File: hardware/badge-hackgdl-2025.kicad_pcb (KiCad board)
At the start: 11 copper layers, 73.4 x 79.5 mm, 61 parts, among them J1 ADDON, J2 Battery, P1 USB_C_Plug_USB2.0, Q1 DMG3415U-7, Q2 MMBT2222A, SW1 ON, SW2 RESET, SW3 BOOT, SW4 RIGHT, SW5 BACK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

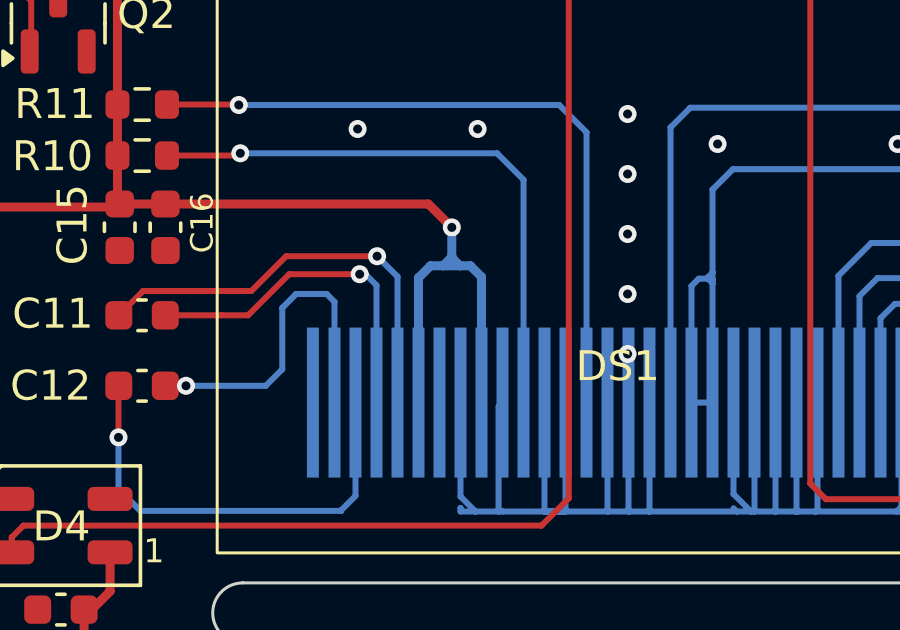
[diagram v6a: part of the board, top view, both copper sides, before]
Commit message: feat(hw): change routes in oled
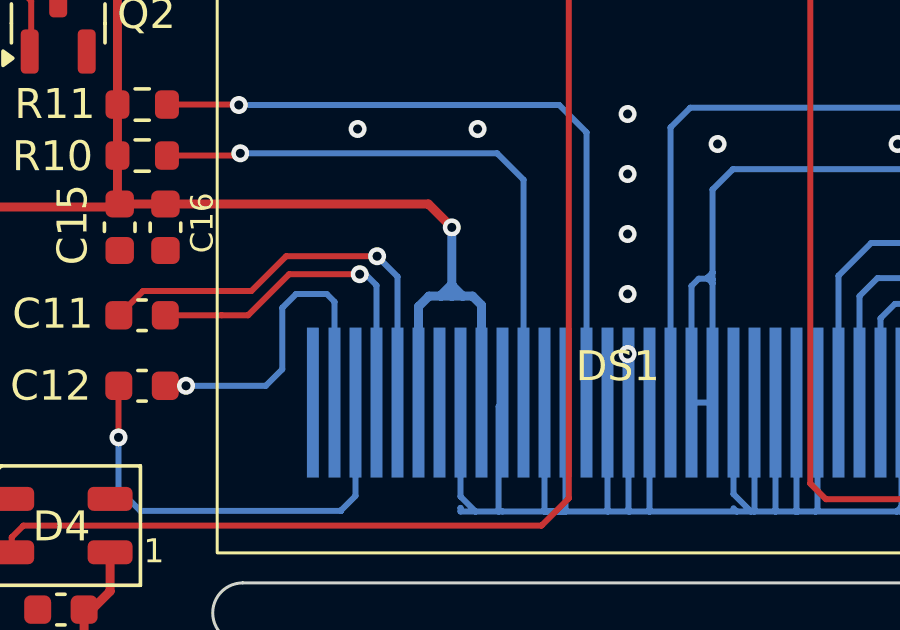
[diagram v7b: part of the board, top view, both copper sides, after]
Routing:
- net +3V3: track 251.2 -> 250.7 mm
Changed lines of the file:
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@@
 		)
 		(embedded_fonts no)
+		(model "${KIPRJMOD}/3dmodels/0.96 OLED - Flat Reverse.stp"
+			(hide yes)
+			(offset
+				(xyz 0 5.5 0)
+			)
+			(scale
+				(xyz 1 1 1)
+			)
+			(rotate
+				(xyz -0 -0 -0)
+			)
+		)
+		(model "${KIPRJMOD}/3dmodels/OLED  0.96 inch 64x128.STEP"
+			(offset
+				(xyz 2 18 -3)
+			)
+			(scale
+				(xyz 1 1 1)
+			)
+			(rotate
+				(xyz -90 -0 -0)
+			)
+		)
 	)
 	(footprint "Capacitor_SMD:C_0603_1608Metric"
@@
 	)
 	(segment
-		(start 128.14 52.74)
-		(end 128.14 52.79)
+		(start 127.78 54.07)
+		(end 127.38 54.07)
 		(width 0.3)
 		(layer "B.Cu")
@@
 	)
 	(segment
-		(start 128.14 51.78)
-		(end 128.14 52.74)
+		(start 128.14 53.68)
+		(end 128.14 54.07)
 		(width 0.3)
 		(layer "B.Cu")
@@
 	)
 	(segment
-		(start 127.85 53.06)
-		(end 127.43 53.06)
+		(start 118.42 88.57)
+		(end 119.54 88.57)
 		(width 0.3)
 		(layer "B.Cu")
@@
 	)
 	(segment
-		(start 127.43 53.06)
-		(end 127.03 53.46)
+		(start 122.945 89.89)
+		(end 122.77 89.715)
 		(width 0.3)
 		(layer "B.Cu")
@@
 	)
 	(segment
-		(start 118.42 88.57)
-		(end 119.54 88.57)
+		(start 128.14 53.71)
+		(end 128.5 54.07)
 		(width 0.3)
 		(layer "B.Cu")
@@
 	)
 	(segment
-		(start 128.14 52.79)
-		(end 128.41 53.06)
+		(start 121.16 89.205)
+		(end 120.175 89.205)
 		(width 0.3)
 		(layer "B.Cu")
@@
 	)
 	(segment
-		(start 128.12 52.79)
-		(end 127.85 53.06)
+		(start 120.175 89.205)
+		(end 119.54 88.57)
 		(width 0.3)
 		(layer "B.Cu")
@@
 	)
 	(segment
-		(start 122.945 89.89)
-		(end 122.77 89.715)
+		(start 124.921189 89.89)
+		(end 122.945 89.89)
 		(width 0.3)
 		(layer "B.Cu")
@@
 	)
 	(segment
-		(start 121.16 89.205)
-		(end 120.175 89.205)
+		(start 128.14 53.68)
+		(end 128.14 53.71)
 		(width 0.3)
 		(layer "B.Cu")
@@
 	)
 	(segment
-		(start 129.13 57.62)
-		(end 129.13 53.43)
+		(start 128.14 51.78)
+		(end 128.14 53.68)
 		(width 0.3)
 		(layer "B.Cu")
@@
 	)
 	(segment
-		(start 120.175 89.205)
-		(end 119.54 88.57)
+		(start 103.419178 53.831476)
+		(end 103.146678 53.558976)
 		(width 0.3)
 		(layer "B.Cu")
@@
 	)
 	(segment
-		(start 127.03 53.46)
-		(end 127.03 57.62)
+		(start 127.78 54.04)
+		(end 127.78 54.07)
 		(width 0.3)
 		(layer "B.Cu")
@@
 	)
 	(segment
-		(start 124.921189 89.89)
-		(end 122.945 89.89)
+		(start 127.03 54.42)
+		(end 127.03 57.62)
 		(width 0.3)
 		(layer "B.Cu")
@@
 	)
 	(segment
-		(start 128.14 52.79)
-		(end 128.12 52.79)
+		(start 128.14 54.07)
+		(end 127.78 54.07)
 		(width 0.3)
 		(layer "B.Cu")
@@
 	)
 	(segment
-		(start 103.419178 53.831476)
-		(end 103.146678 53.558976)
+		(start 122.77 89.715)
+		(end 121.67 89.715)
 		(width 0.3)
 		(layer "B.Cu")
@@
 	)
 	(segment
-		(start 128.76 53.06)
-		(end 128.41 53.06)
+		(start 129.13 54.37)
+		(end 128.83 54.07)
 		(width 0.3)
 		(layer "B.Cu")
@@
 	)
 	(segment
-		(start 122.77 89.715)
-		(end 121.67 89.715)
+		(start 151.2 85.68)
+		(end 149.135 85.68)
 		(width 0.3)
 		(layer "B.Cu")
@@
 	)
 	(segment
-		(start 128.01 53.06)
-		(end 127.85 53.06)
+		(start 129.13 57.62)
+		(end 129.13 54.37)
 		(width 0.3)
 		(layer "B.Cu")
@@
 	)
 	(segment
-		(start 151.2 85.68)
-		(end 149.135 85.68)
+		(start 128.83 54.07)
+		(end 128.5 54.07)
 		(width 0.3)
 		(layer "B.Cu")
@@
 	)
 	(segment
-		(start 117.85 88)
-		(end 118.42 88.57)
+		(start 127.38 54.07)
+		(end 127.03 54.42)
 		(width 0.3)
 		(layer "B.Cu")
@@
 	)
 	(segment
-		(start 128.14 52.74)
-		(end 128.14 52.93)
+		(start 117.85 88)
+		(end 118.42 88.57)
 		(width 0.3)
 		(layer "B.Cu")
@@
 	)
 	(segment
-		(start 128.41 53.06)
-		(end 128.01 53.06)
+		(start 128.14 53.68)
+		(end 127.78 54.04)
 		(width 0.3)
 		(layer "B.Cu")
@@
 	)
 	(segment
-		(start 129.13 53.43)
-		(end 128.76 53.06)
+		(start 128.5 54.07)
+		(end 128.14 54.07)
 		(width 0.3)
 		(layer "B.Cu")

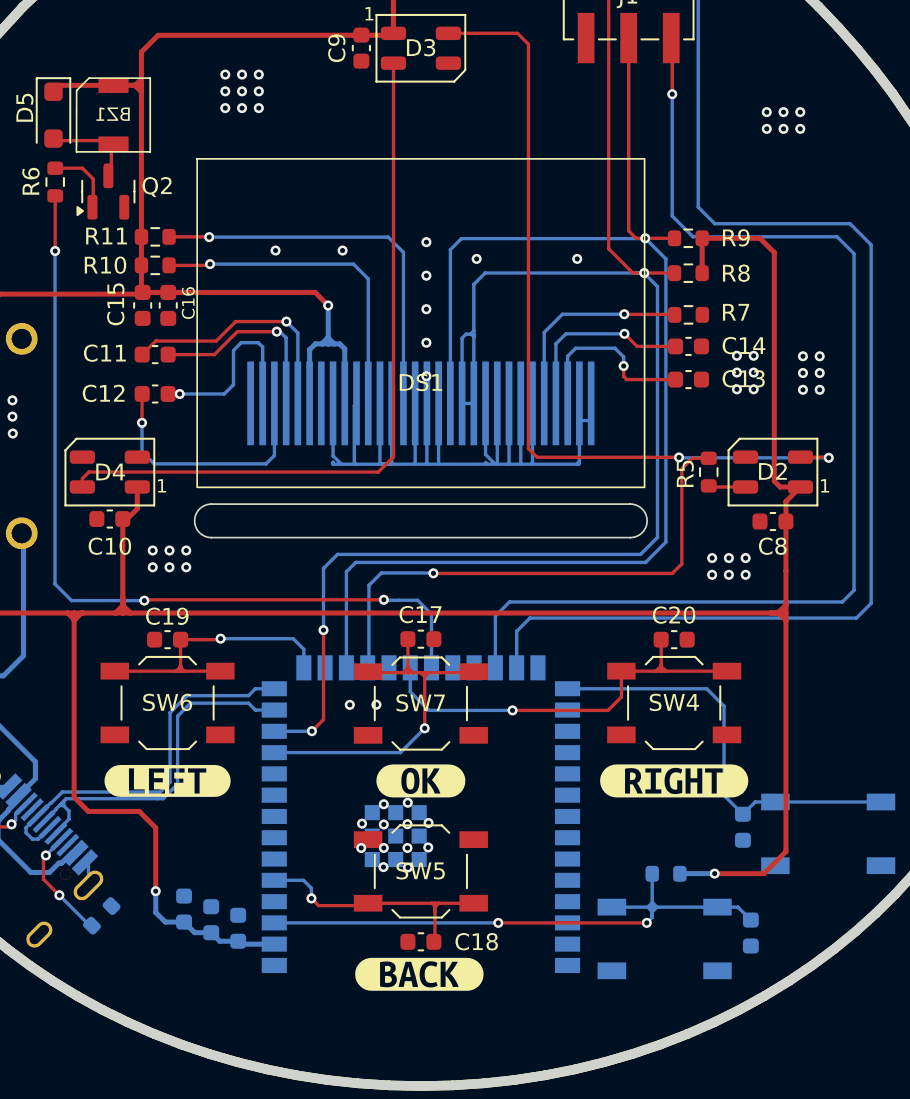
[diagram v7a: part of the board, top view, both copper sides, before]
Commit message: refactor(hw): move buttons
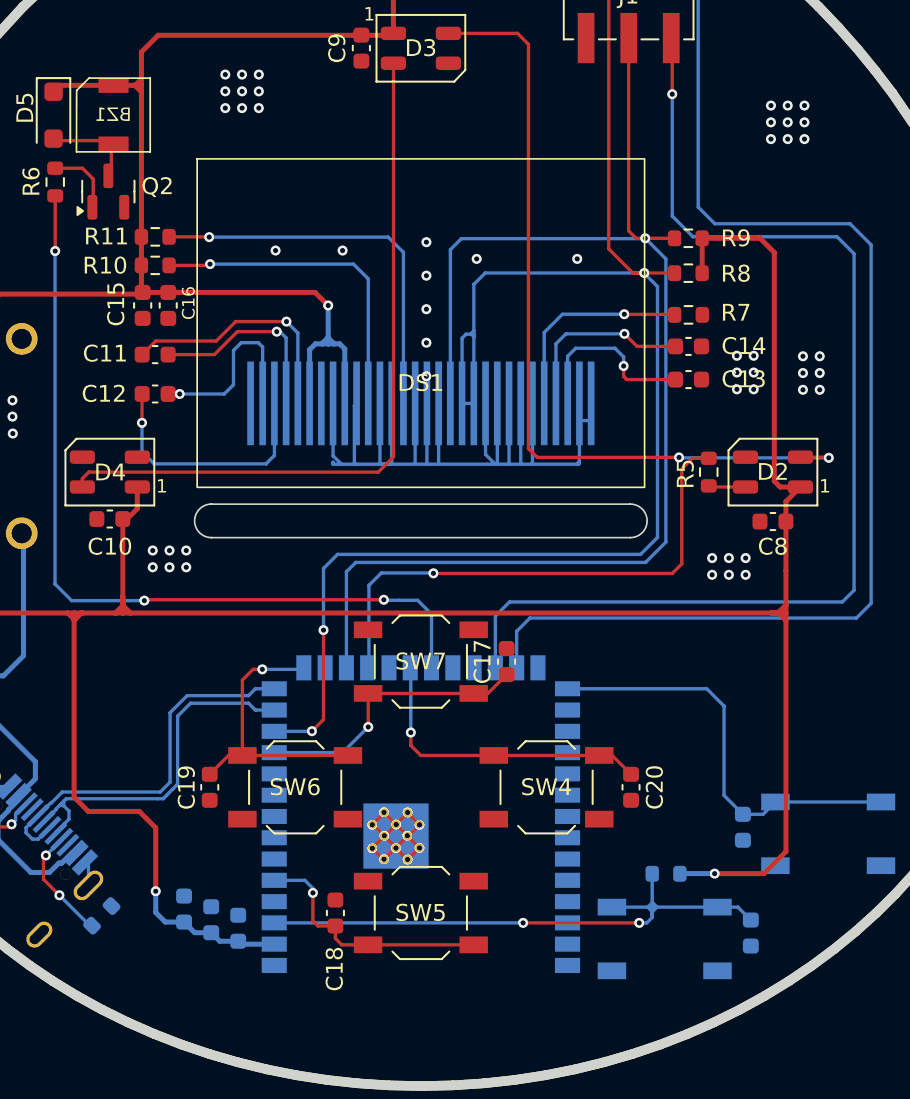
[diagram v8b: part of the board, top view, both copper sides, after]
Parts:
- removed kibuzzard-6786EBF3: G***, kibuzzard-6786EBF3
- removed kibuzzard-6786EC12: G***, kibuzzard-6786EC12
- removed kibuzzard-6786EC27: G***, kibuzzard-6786EC27
- removed kibuzzard-6786EC60: G***, kibuzzard-6786EC60
- moved C20 9.18 mm to (146.2, 80.5), turned to -90 degrees
- moved C19 9.16 mm to (121.1, 80.5), turned to -90 degrees
- moved SW4 9.13 mm to (141.2, 80.5)
- moved SW6 9.13 mm to (126.2, 80.5)
- moved C18 5.38 mm to (128.6, 88.0), turned to 90 degrees
- moved C17 5.29 mm to (138.8, 73.0), turned to 90 degrees
- moved SW7 2.50 mm to (133.7, 73.0), turned to 0 degrees
- moved SW5 2.48 mm to (133.7, 88.0)
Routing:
- net GND: track 73.4 -> 99.6 mm, vias 92 -> 93
- net /RIGHT: track 25.5 -> 18.5 mm
- net /MIDDLE: track 23.0 -> 17.0 mm
- net /BACK: track 16.2 -> 15.1 mm
- net /LEFT: track 17.8 -> 17.2 mm
